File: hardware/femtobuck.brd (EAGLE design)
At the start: 10.1 x 31.1 mm, 11 parts

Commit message: Incorporate changes from review
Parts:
- added JP2: M02PTH, SparkFun-Connectors:1X02
- moved FRAME1 10.2 mm to (11.4, -20.3)
- moved JP1 7.24 mm to (1.27, 31.8)
- moved LOGO2 7.17 mm to (9.78, 24.4)
- moved C1 5.08 mm to (8.89, 22.2)
- moved L1 5.08 mm to (5.08, 16.5)
- moved LOGO1 5.08 mm to (2.03, 26.3)
- moved R1 5.08 mm to (8.89, 26.0)
- moved U1 5.08 mm to (5.08, 22.0)
- moved CH1 5.08 mm to (3.30, 9.27)
- moved C2 5.08 mm to (3.81, 26.9)
- moved D1 5.08 mm to (1.91, 22.9)
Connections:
- net OUT+: now also JP2.1
- net OUT-: now also JP2.2
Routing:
- net GND: track 19.9 -> 24.2 mm
- net OUT-: track 9.65 -> 12.9 mm
- net OUT+: track 18.3 -> 21.5 mm
- net CTRL_CH1: track 12.8 -> 15.0 mm
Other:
- board size 10.1 x 31.1 mm -> 10.2 x 37.5 mm
- board text added: "+ LED -"
- board text added: "- LED +"
- board text added: "M. Hord"
- board text removed: "M. Hord/E. Zonca"
- board text removed: "OUT+"
- board text removed: "OUT-"

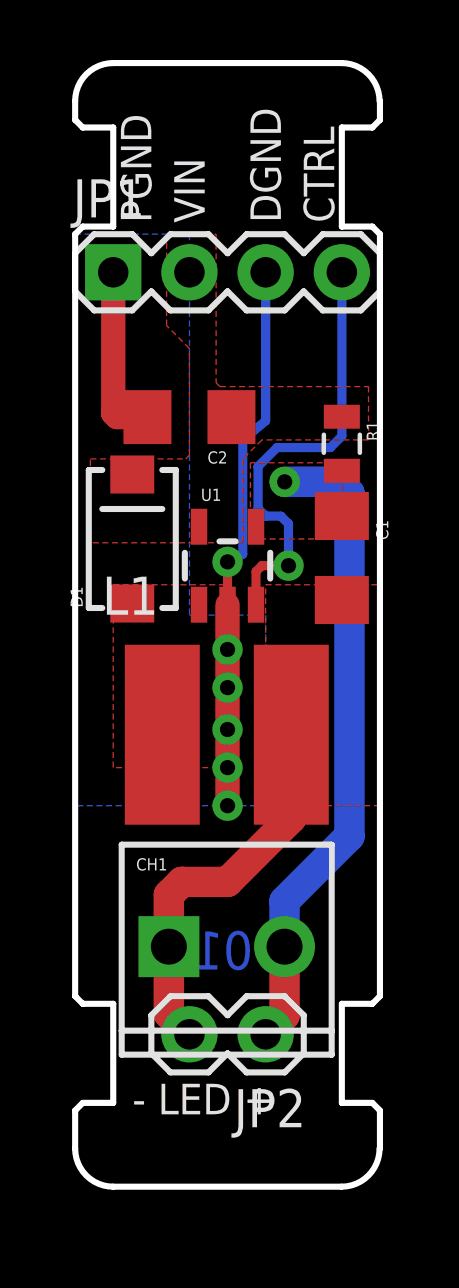
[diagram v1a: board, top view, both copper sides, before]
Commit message: Small updates for production
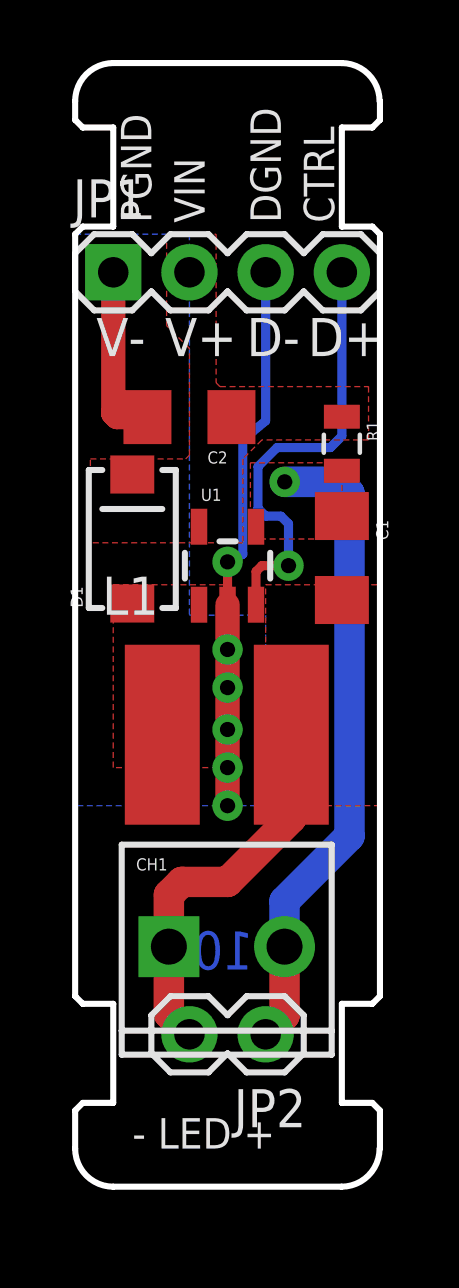
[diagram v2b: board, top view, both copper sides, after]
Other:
- board text added: "D+"
- board text added: "D-"
- board text added: "V+"
- board text added: "V-"
- board text added: "v10"
- board text removed: "v01"
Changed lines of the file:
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@@
 <text x="6.35" y="33.401" size="1.016" layer="21" font="vector" ratio="15" rot="R90" align="center-left">DGND</text>
 <text x="8.128" y="33.401" size="1.016" layer="21" font="vector" ratio="15" rot="R90" align="center-left">CTRL</text>
-<text x="6.858" y="9.144" size="1.27" layer="16" font="vector" ratio="15" rot="MR0" align="center-left">v01</text>
+<text x="6.858" y="9.144" size="1.27" layer="16" font="vector" ratio="15" rot="MR0" align="center-left">v10</text>
 <text x="2.032" y="24.003" size="1.6764" layer="22" font="vector" ratio="15" rot="SMR270" align="center-left">FemtoBuck</text>
 <text x="2.032" y="36.83" size="1.016" layer="22" font="vector" ratio="15" rot="SMR270" align="center-left">PGND</text>
@@
 <text x="6.35" y="36.957" size="1.016" layer="22" font="vector" ratio="15" rot="SMR270" align="center-left">DGND</text>
 <text x="8.128" y="36.83" size="1.016" layer="22" font="vector" ratio="15" rot="SMR270" align="center-left">CTRL</text>
-<text x="4.826" y="27.94" size="0.8128" layer="22" font="vector" ratio="15" rot="SMR270" align="center-left">6-36V 350mA
-CC LED Driver</text>
+<text x="3.937" y="28.448" size="0.8128" layer="22" font="vector" ratio="15" rot="SMR270" align="center-left">6-36V 350mA CC LED Driver</text>
 <text x="41.91" y="-20.32" size="1.778" layer="51" ratio="15">M. Hord</text>
 <wire x1="0" y1="37.465" x2="0" y2="36.83" width="0.2032" layer="20"/>
@@
 <wire x1="9.906" y1="4.064" x2="10.16" y2="3.81" width="0.2032" layer="20"/>
 <wire x1="10.16" y1="3.81" x2="10.16" y2="2.54" width="0.2032" layer="20"/>
-<text x="1.905" y="3.683" size="1.016" layer="21" font="vector" ratio="15">- LED +</text>
-<text x="8.255" y="3.683" size="1.016" layer="22" font="vector" ratio="15" rot="MR0">+ LED -</text>
+<text x="1.905" y="2.54" size="1.016" layer="21" font="vector" ratio="15">- LED +</text>
+<text x="8.255" y="2.54" size="1.016" layer="22" font="vector" ratio="15" rot="MR0">+ LED -</text>
+<text x="1.524" y="28.956" size="1.27" layer="21" font="vector" ratio="15" align="bottom-center">V-</text>
+<text x="4.191" y="28.956" size="1.27" layer="21" font="vector" ratio="15" align="bottom-center">V+</text>
+<text x="6.604" y="28.956" size="1.27" layer="21" font="vector" ratio="15" align="bottom-center">D-</text>
+<text x="9.017" y="28.956" size="1.27" layer="21" font="vector" ratio="15" align="bottom-center">D+</text>
+<text x="1.27" y="28.956" size="1.27" layer="22" font="vector" ratio="15" rot="MR0" align="bottom-center">V-</text>
+<text x="3.937" y="28.956" size="1.27" layer="22" font="vector" ratio="15" rot="MR0" align="bottom-center">V+</text>
+<text x="6.35" y="28.956" size="1.27" layer="22" font="vector" ratio="15" rot="MR0" align="bottom-center">D-</text>
+<text x="8.763" y="28.956" size="1.27" layer="22" font="vector" ratio="15" rot="MR0" align="bottom-center">D+</text>
 </plain>
 <attributes>
@@
 </board>
 </drawing>
-<compatibility>
-<note version="6.3" minversion="6.2.2" severity="warning">
-Since Version 6.2.2 text objects can contain more than one line,
-which will not be processed correctly with this version.
-</note>
-</compatibility>
 </eagle>

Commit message: added board fiducials
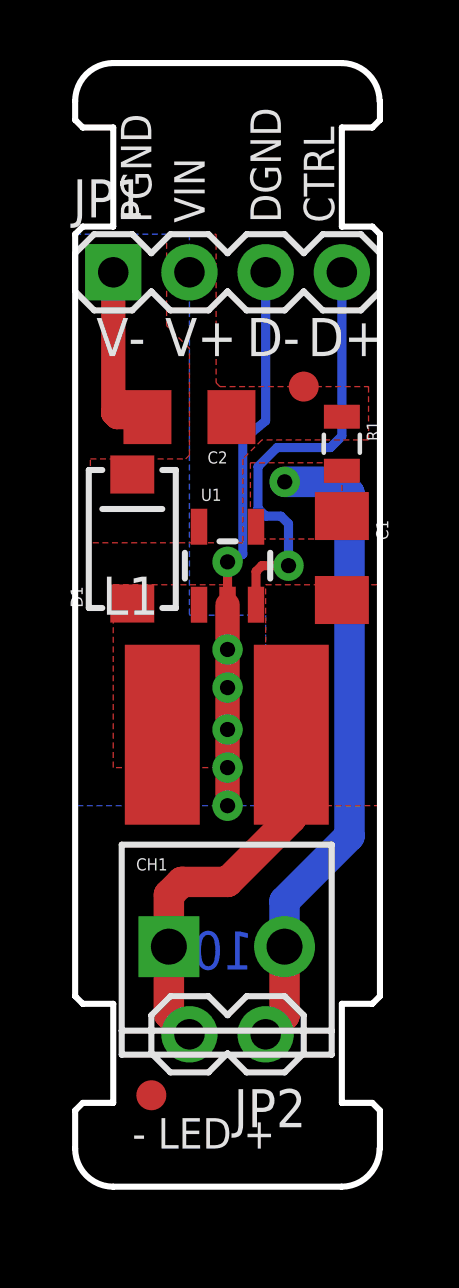
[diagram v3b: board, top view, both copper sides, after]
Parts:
- added FID1, FID2: FIDUCIAL1X2, SparkFun-Aesthetics:FIDUCIAL-1X2
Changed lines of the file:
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@@
 <setting verticaltext="up"/>
 </settings>
-<grid distance="0.05" unitdist="inch" unit="inch" style="lines" multiple="1" display="yes" altdistance="0.005" altunitdist="inch" altunit="inch"/>
+<grid distance="0.01" unitdist="inch" unit="inch" style="lines" multiple="1" display="yes" altdistance="0.001" altunitdist="inch" altunit="inch"/>
 <layers>
 <layer number="1" name="Top" color="4" fill="1" visible="yes" active="yes"/>
-<layer number="2" name="Route2" color="1" fill="3" visible="no" active="yes"/>
-<layer number="15" name="Route15" color="4" fill="6" visible="no" active="yes"/>
+<layer number="2" name="Route2" color="1" fill="3" visible="yes" active="yes"/>
+<layer number="15" name="Route15" color="4" fill="6" visible="yes" active="yes"/>
 <layer number="16" name="Bottom" color="1" fill="1" visible="yes" active="yes"/>
 <layer number="17" name="Pads" color="2" fill="1" visible="yes" active="yes"/>
@@
 <layer number="19" name="Unrouted" color="6" fill="1" visible="yes" active="yes"/>
 <layer number="20" name="Dimension" color="6" fill="1" visible="yes" active="yes"/>
-<layer number="21" name="tPlace" color="16" fill="1" visible="yes" active="yes"/>
-<layer number="22" name="bPlace" color="14" fill="1" visible="yes" active="yes"/>
+<layer number="21" name="tPlace" color="6" fill="1" visible="yes" active="yes"/>
+<layer number="22" name="bPlace" color="6" fill="1" visible="yes" active="yes"/>
 <layer number="23" name="tOrigins" color="15" fill="1" visible="yes" active="yes"/>
 <layer number="24" name="bOrigins" color="15" fill="1" visible="yes" active="yes"/>
-<layer number="25" name="tNames" color="7" fill="1" visible="no" active="yes"/>
-<layer number="26" name="bNames" color="7" fill="1" visible="no" active="yes"/>
-<layer number="27" name="tValues" color="7" fill="1" visible="no" active="yes"/>
-<layer number="28" name="bValues" color="7" fill="1" visible="no" active="yes"/>
-<layer number="29" name="tStop" color="7" fill="3" visible="no" active="yes"/>
-<layer number="30" name="bStop" color="7" fill="6" visible="no" active="yes"/>
-<layer number="31" name="tCream" color="7" fill="4" visible="no" active="yes"/>
-<layer number="32" name="bCream" color="7" fill="5" visible="no" active="yes"/>
-<layer number="39" name="tKeepout" color="4" fill="11" visible="no" active="yes"/>
-<layer number="40" name="bKeepout" color="1" fill="11" visible="no" active="yes"/>
-<layer number="41" name="tRestrict" color="4" fill="10" visible="no" active="yes"/>
-<layer number="42" name="bRestrict" color="1" fill="10" visible="no" active="yes"/>
-<layer number="43" name="vRestrict" color="2" fill="10" visible="no" active="yes"/>
-<layer number="44" name="Drills" color="7" fill="1" visible="no" active="yes"/>
+<layer number="25" name="tNames" color="7" fill="1" visible="yes" active="yes"/>
+<layer number="26" name="bNames" color="7" fill="1" visible="yes" active="yes"/>
+<layer number="27" name="tValues" color="7" fill="1" visible="yes" active="yes"/>
+<layer number="28" name="bValues" color="7" fill="1" visible="yes" active="yes"/>
+<layer number="29" name="tStop" color="7" fill="3" visible="yes" active="yes"/>
+<layer number="30" name="bStop" color="7" fill="6" visible="yes" active="yes"/>
+<layer number="31" name="tCream" color="7" fill="4" visible="yes" active="yes"/>
+<layer number="32" name="bCream" color="7" fill="5" visible="yes" active="yes"/>
+<layer number="39" name="tKeepout" color="4" fill="11" visible="yes" active="yes"/>
+<layer number="40" name="bKeepout" color="1" fill="11" visible="yes" active="yes"/>
+<layer number="41" name="tRestrict" color="4" fill="10" visible="yes" active="yes"/>
+<layer number="42" name="bRestrict" color="1" fill="10" visible="yes" active="yes"/>
+<layer number="43" name="vRestrict" color="2" fill="10" visible="yes" active="yes"/>
+<layer number="44" name="Drills" color="7" fill="1" visible="yes" active="yes"/>
 <layer number="45" name="Holes" color="7" fill="1" visible="yes" active="yes"/>
-<layer number="46" name="Milling" color="3" fill="1" visible="no" active="yes"/>
+<layer number="46" name="Milling" color="3" fill="1" visible="yes" active="yes"/>
 <layer number="51" name="tDocu" color="6" fill="1" visible="yes" active="yes"/>
-<layer number="52" name="bDocu" color="7" fill="1" visible="no" active="yes"/>
+<layer number="52" name="bDocu" color="7" fill="1" visible="yes" active="yes"/>
 <layer number="3" name="Route3" color="4" fill="3" visible="no" active="no"/>
 <layer number="4" name="Route4" color="1" fill="4" visible="no" active="no"/>
@@
 <element name="LOGO2" library="SparkFun-Aesthetics" package="SFE_LOGO_NAME_FLAME_.1" value="SFE_LOGO_NAME_FLAME.1_INCH" x="9.779" y="24.384" rot="MR270"/>
 <element name="JP2" library="SparkFun-Connectors" package="1X02" value="M02PTH" x="6.35" y="6.35" rot="R180"/>
+<element name="FID1" library="SparkFun-Aesthetics" package="FIDUCIAL-1X2" value="FIDUCIAL1X2" x="7.62" y="27.94"/>
+<element name="FID2" library="SparkFun-Aesthetics" package="FIDUCIAL-1X2" value="FIDUCIAL1X2" x="2.54" y="4.318"/>
 </elements>
 <signals>

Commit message: Added 2nd sense resistor, jumper
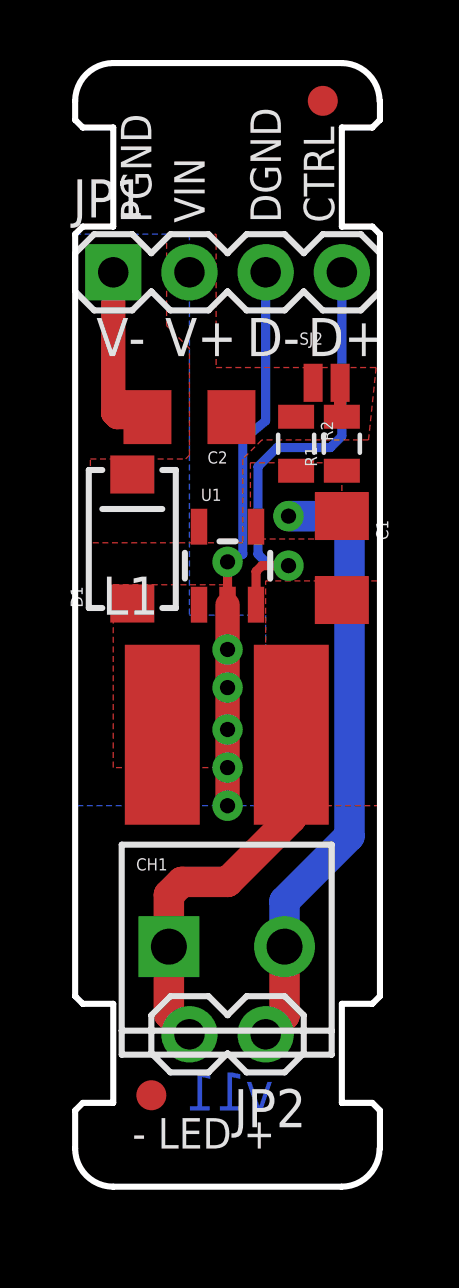
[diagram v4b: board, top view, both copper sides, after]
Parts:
- added R2: 0.3R, SparkFun-Resistors:0805
- added SJ2: NO Jumper, SparkFun-Passives:PAD-JUMPER-2-NO_NO_SILK
- moved FID1 9.55 mm to (8.26, 37.5)
- turned R1 to 90 degrees
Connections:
- new net N$1: R1.2, SJ2.2
- net OUT+: now also R1.1, R2.2; no longer R1.2
- net VIN: now also R2.1, SJ2.1; no longer R1.1
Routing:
- net OUT+: track 21.5 -> 20.2 mm
- net N$1: track 0.00 -> 1.16 mm
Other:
- board text added: "6-36V 333/667mA"
- board text added: "LED Driver"
- board text added: "v11"
- board text removed: "6-36V 350mA CC LED Driver"
- board text removed: "v10"
